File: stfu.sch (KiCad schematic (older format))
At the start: 88 parts, among them K1 FTDI, K2 ISP, K3 I2C, K4 SERVO, K5 V_SEL, P1 CONN_1, P2 CONN_1, P3 HAND_HI, P4 HAND_LO, P5 HAND_HI, P6 HAND_LO, P7 BATT_12V, P8 CONN_1, P9 CONN_1, Q1 PNP, SW2 RST, SW3 SW_ENT, U1 ATMEGA328-P, U2 HEF4051B, U3 ULN2803, U4 7809, U5 7805, X1 16MHz

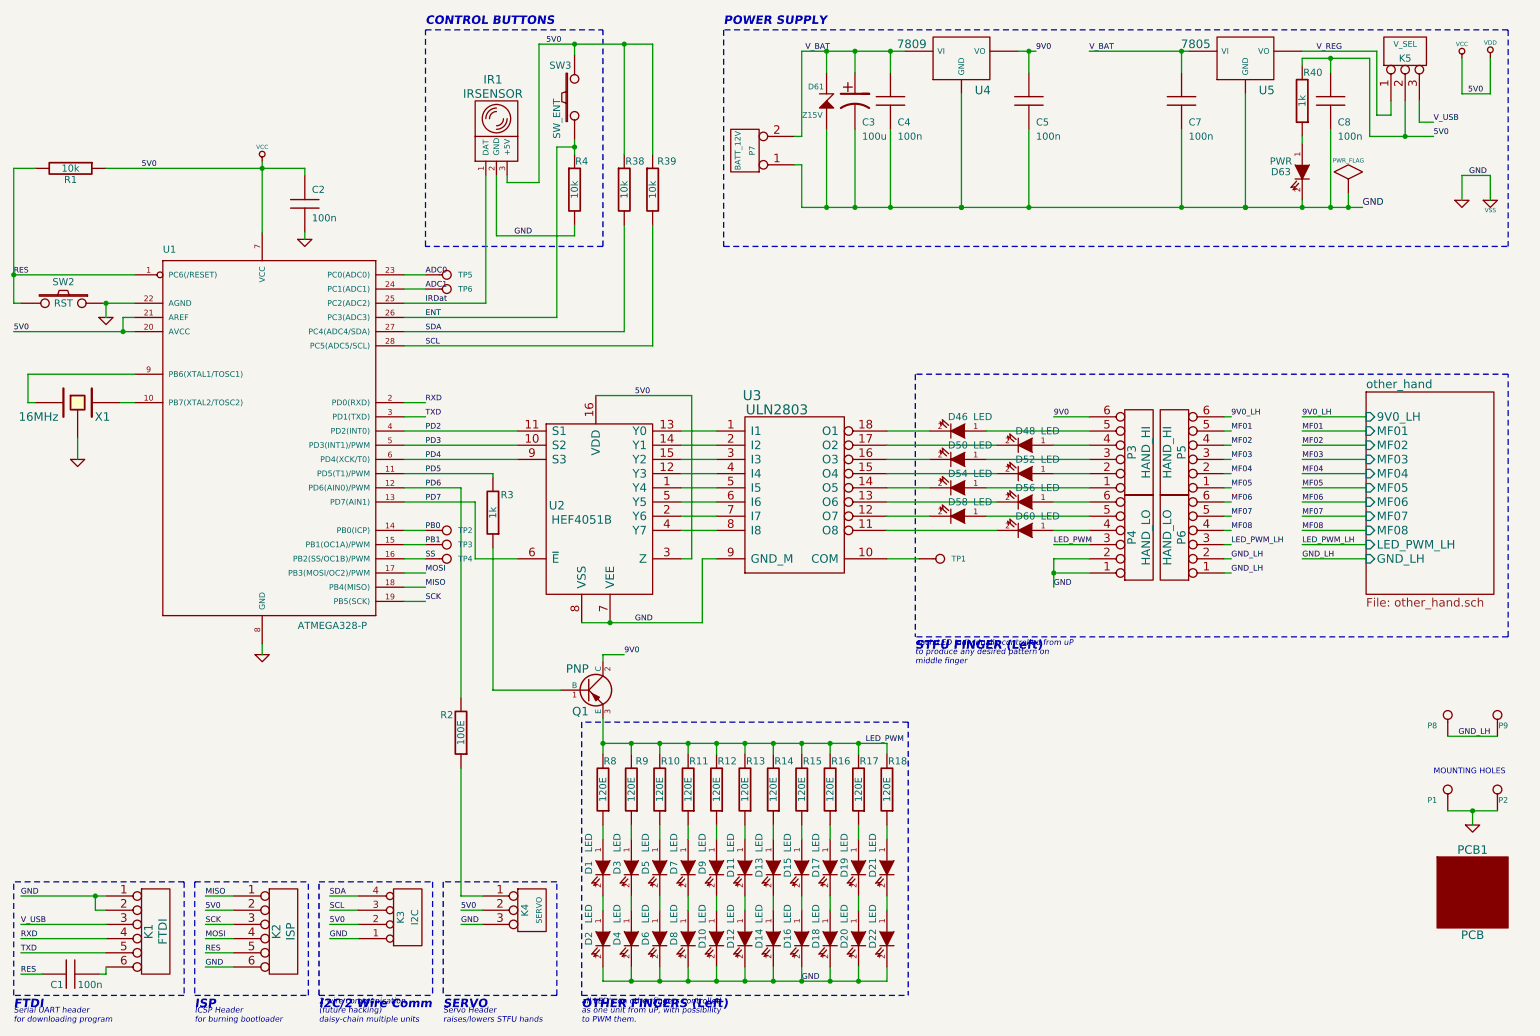
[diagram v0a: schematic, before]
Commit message: WiP - decided to add a IR Transmitter in the spare available board space.
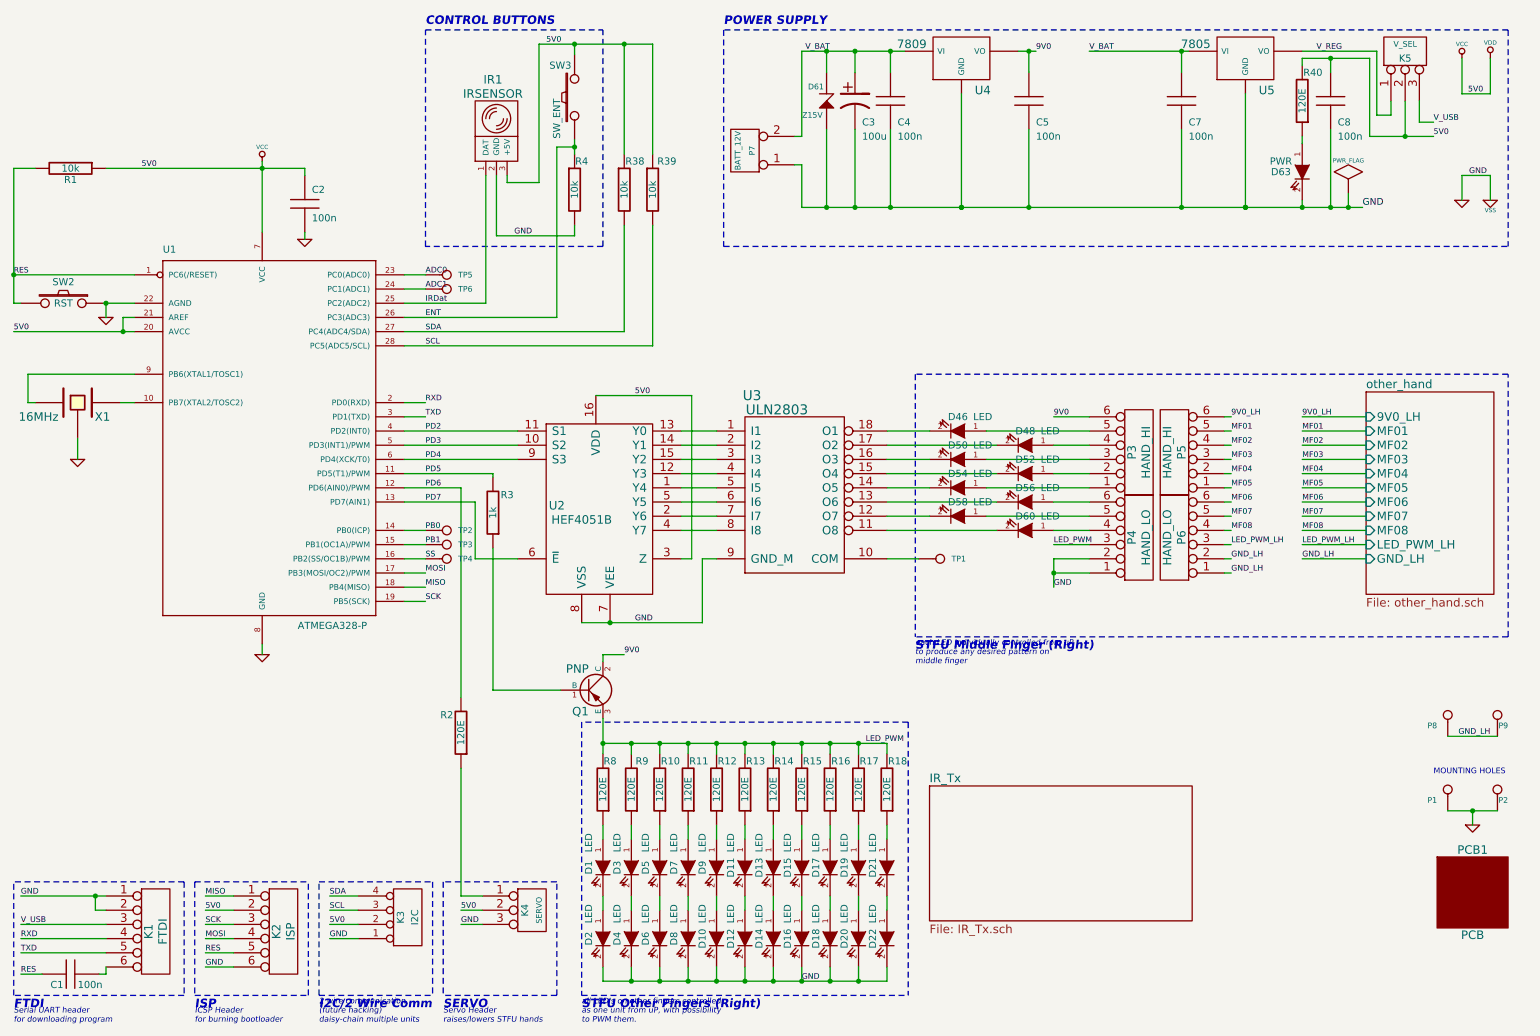
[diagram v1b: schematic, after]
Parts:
- C1, C2, C4, C5, C7, C8: footprint C2 -> c_0805
- C3: footprint CP_5x11mm -> C_ELCO_SMD
- D1, D10, D11, D12, D13, D14, D15, D16, D17, D18, D19, D2, D20, D21, D22, D3, D4, D46, D48, D5, D50, D52, D54, D56, D58, D6, D60, D7, D8, D9: footprint (none) -> d_1206
- D61: footprint DO-35_Vert -> SOD323F
- D63: footprint led_5mm_blue -> d_0805
- IR1: footprint (none) -> pin_strip_3
- K1: footprint pin_strip_6 -> Header_FTDI
- K2: footprint pin_strip_3x2 -> Header_ICSP
- K4: footprint pin_strip_3 -> Header_Ser
- K5: footprint pin_strip_3 -> Header_V_SEL
- P3, P4, P5, P6: footprint (none) -> pin_strip_6b
- P7: footprint (none) -> bornier2
- Q1: footprint (none) -> sot223
- R1, R38, R39, R4: footprint RC03 -> r_0805
- R2: value 100E -> 120E
- R40: value 1k -> 120E; footprint RC03 -> r_0805
- TP1, TP2, TP3, TP4, TP5, TP6: footprint (none) -> I/O
- U1: footprint dil_28-300_socket -> DIP-28__300_ELL
- U2: footprint (none) -> SO16E
- U3: footprint (none) -> SO18W
- U4, U5: footprint TO-220_Vertical -> DPAK-3
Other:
- note added: "STFU Middle Finger (Right)"
- note added: "STFU Other Fingers (Right)"
- note removed: "OTHER FINGERS (Left)"
- note removed: "STFU FINGER (Left)"

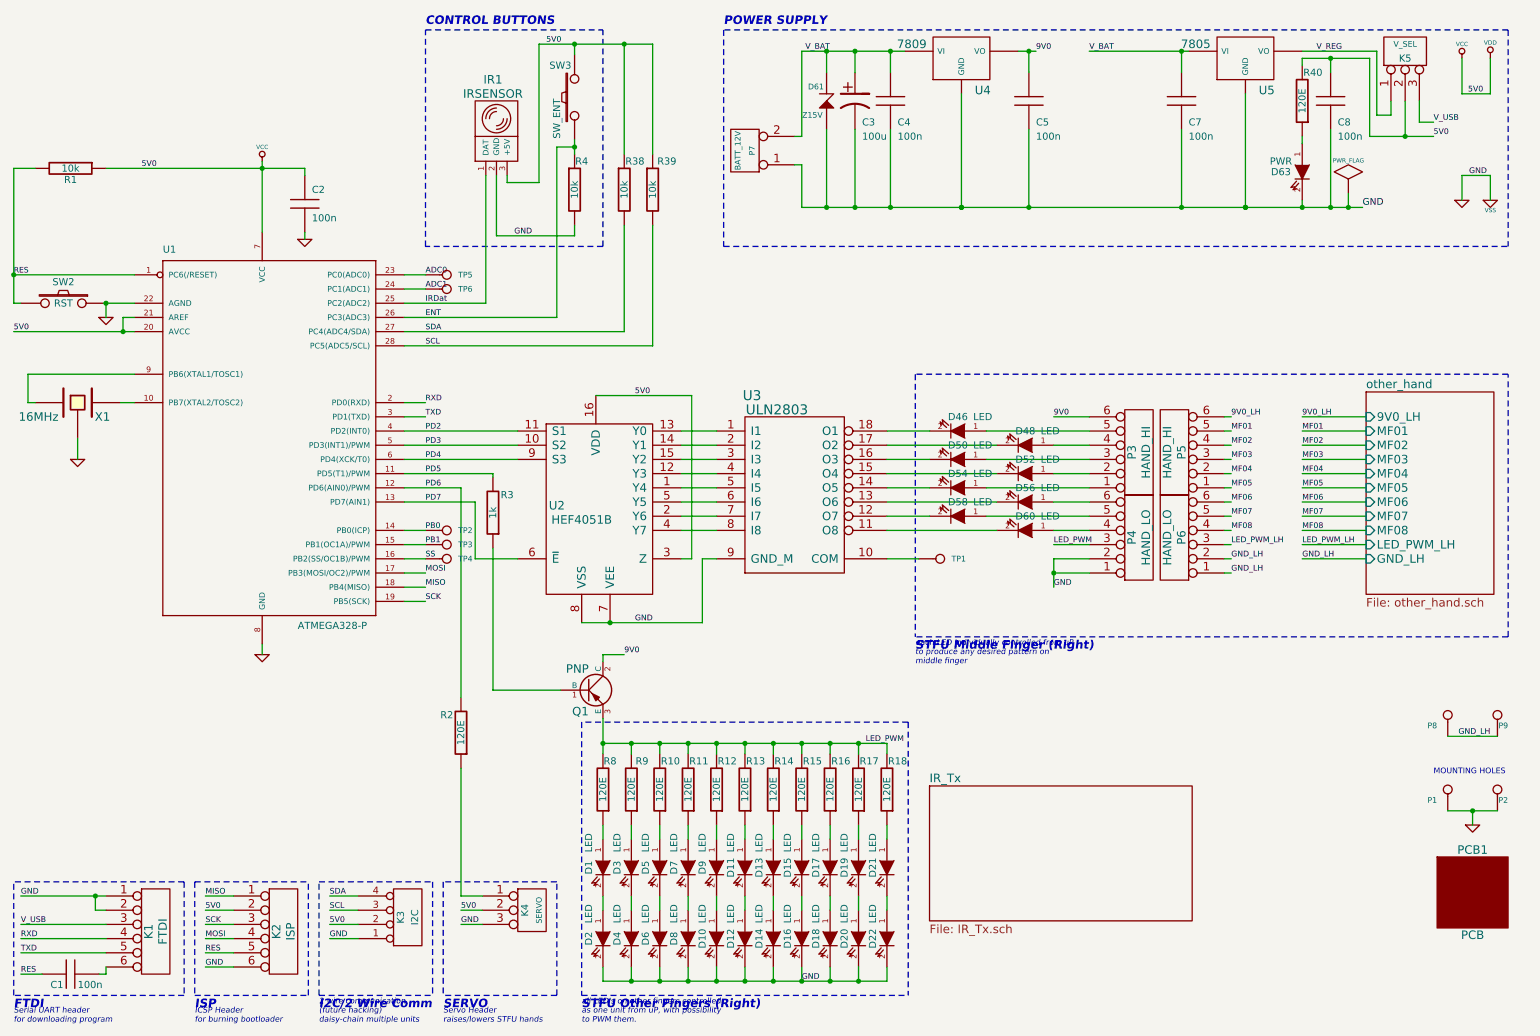
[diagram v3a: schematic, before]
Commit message: WiP - track cleanup and optimization, Legend clean up etc.
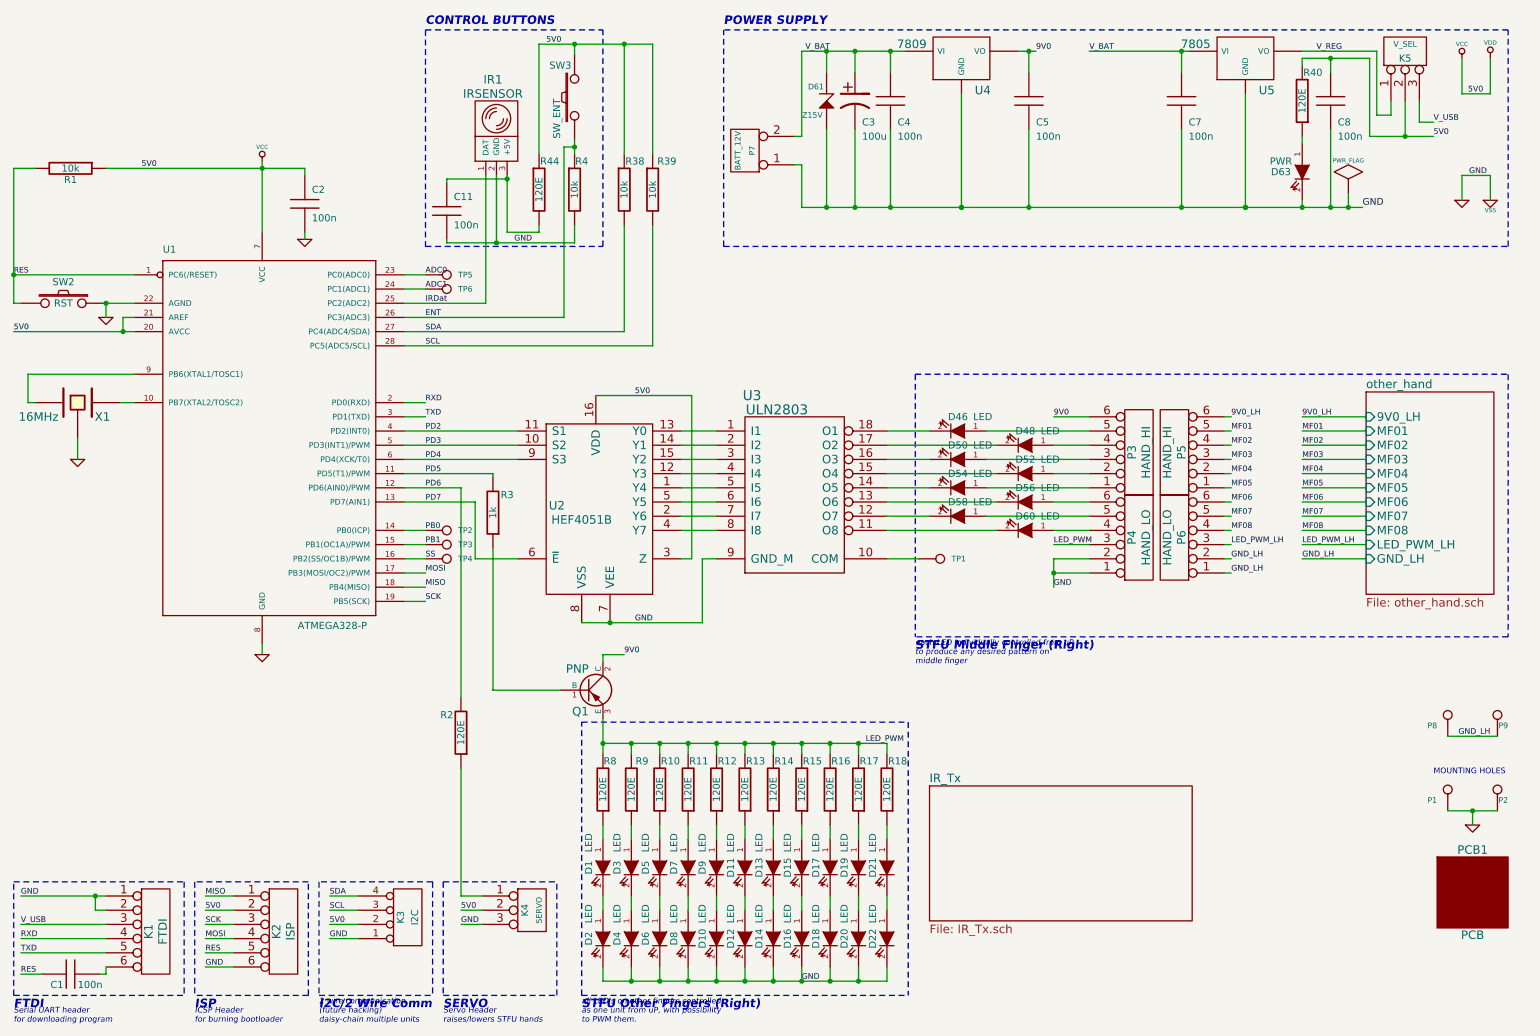
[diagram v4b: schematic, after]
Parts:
- added C11: 100n, c_0805, symbol C
- added R44: 120E, r_0805, symbol R
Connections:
- net GND: now also C11.2
- net VCC: now also R44.1; no longer IR1.3 (+5V)
- new net: C11.1, IR1.3 (+5V), R44.2
